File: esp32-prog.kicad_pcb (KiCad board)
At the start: 2 copper layers, 55 x 30 mm, 65 parts, among them J1 TYPE-C-31-M-12, J2 Conn-02x05_PZ254-2-05-Z-8.5, Q1 AO3401A, Q2 AO3401A, Q3 AO3400A, Q4 AO3400A, SW1 SW_DIP_x02_50mil_1.27mm_TP-02, U1 LD39200DPUR, U2 CP2102-GMR, U3 TI_SN74LVC1G125DRYR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

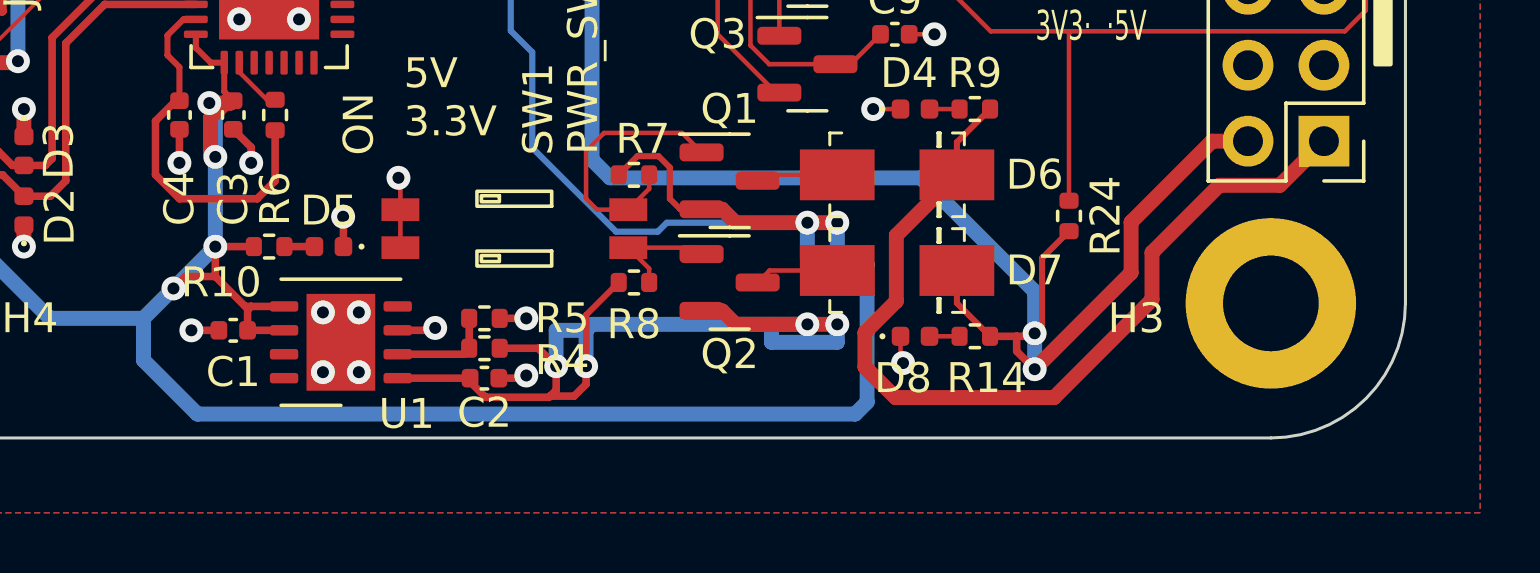
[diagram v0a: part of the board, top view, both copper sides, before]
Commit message: address the incorect pinout of the LD39200DPUR
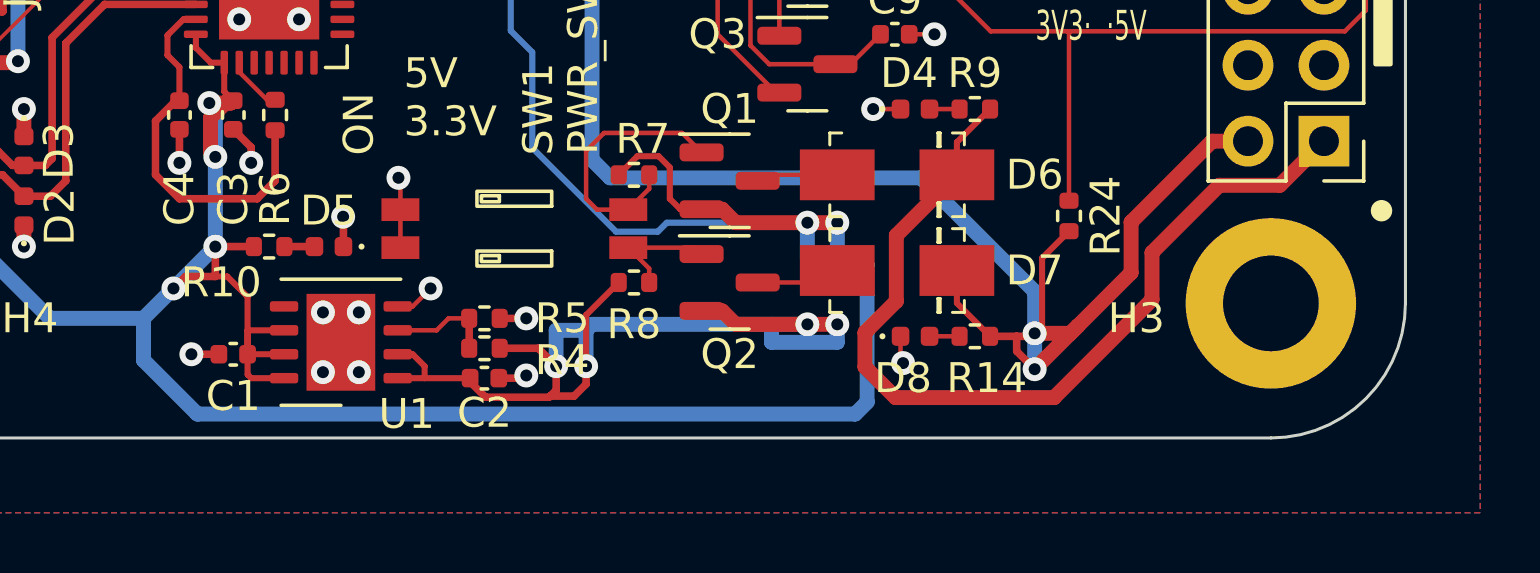
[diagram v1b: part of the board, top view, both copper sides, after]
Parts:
- moved C1 0.80 mm to (90.8, 84.7)
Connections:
- R4 pad 2: Net-(U1-ADJ) -> Net-(U1-GND)
- R5 pad 1: Net-(U1-ADJ) -> Net-(U1-GND)
- U1 pad 2: Net-(U1-ADJ) -> +3.3VA
- U1 pad 3: GND -> Net-(U1-GND)
- U1 pad 4: unconnected-(U1-PG-Pad4) -> GND
- U1 pad 5: VBUS -> unconnected-(U1-PG-Pad5)
- U1 pad 7: (no net) -> VBUS
- U1 pad 8: (no net) -> VBUS
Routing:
- net VBUS: track 127.3 -> 131.1 mm
- net Net-(U1-GND): track 0.00 -> 3.56 mm
- net Net-(U1-ADJ): track 3.47 -> 0.00 mm
- net +3.3V: track 80.6 -> 82.2 mm
- net +3.3VA: track 32.8 -> 34.2 mm
- net Net-(Q2-D): track 2.83 -> 2.26 mm
